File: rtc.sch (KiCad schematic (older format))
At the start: 0 parts

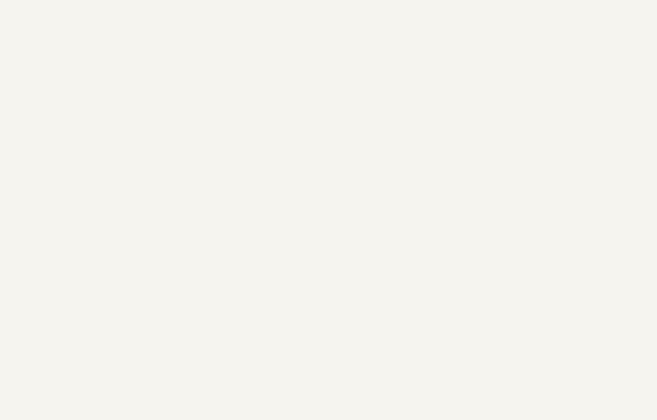
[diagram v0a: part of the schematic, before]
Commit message: Added some footprints. Basic board outline.
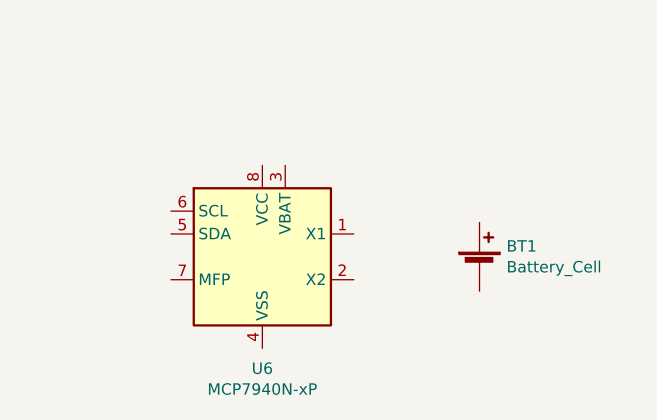
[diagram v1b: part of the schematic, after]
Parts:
- added BT1: Battery_Cell, Battery:BatteryHolder_Keystone_103_1x20mm, symbol Device:Battery_Cell
- added U6: MCP7940N-xP, Package_DIP:DIP-8_W7.62mm, symbol Timer:MCP7940N-xP
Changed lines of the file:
@@
 $Descr A4 11693 8268
 encoding utf-8
-Sheet 11 11
+Sheet 10 11
 Title "Neotron 32K"
 Date "2019-12-08"
@@
 Text HLabel 1400 1550 0    50   Input ~ 0
 MCU_I2C_SCL
+$Comp
+L Timer:MCP7940N-xP U6
+U 1 1 5E0F47D7
+P 5650 3350
+F 0 "U6" H 5650 2861 50  0000 C CNN
+F 1 "MCP7940N-xP" H 5650 2770 50  0000 C CNN
+F 2 "Package_DIP:DIP-8_W7.62mm" H 5650 3350 50  0001 C CNN
+F 3 "http://ww1.microchip.com/downloads/en/DeviceDoc/20005010F.pdf" H 5650 3350 50  0001 C CNN
+	1    5650 3350
+	1    0    0    -1
+$EndComp
+$Comp
+L Device:Battery_Cell BT1
+U 1 1 5E0F507E
+P 6600 3400
+F 0 "BT1" H 6718 3496 50  0000 L CNN
+F 1 "Battery_Cell" H 6718 3405 50  0000 L CNN
+F 2 "Battery:BatteryHolder_Keystone_103_1x20mm" V 6600 3460 50  0001 C CNN
+F 3 "~" V 6600 3460 50  0001 C CNN
+	1    6600 3400
+	1    0    0    -1
+$EndComp
 $EndSCHEMATC

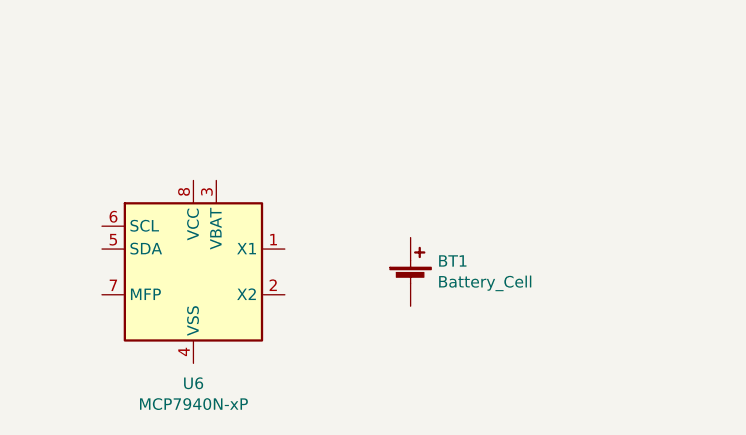
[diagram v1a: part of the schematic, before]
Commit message: Completed Power, SD, MIDI, Parallel and Joystick sheets.
Switch to sheet based 100x part numbering.
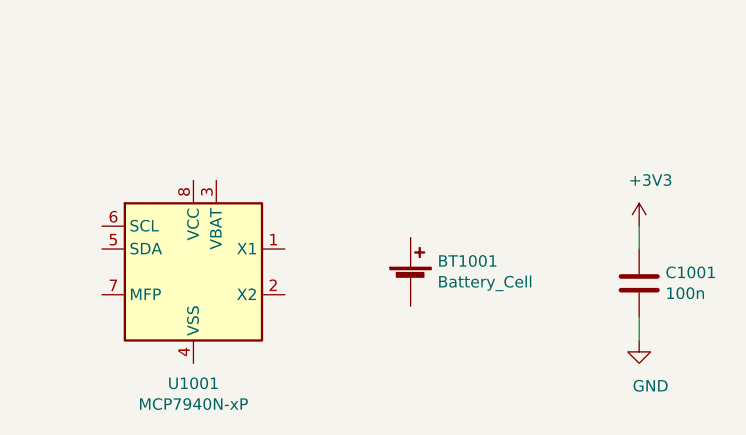
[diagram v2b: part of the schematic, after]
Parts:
- added C1001: 100n, Capacitor_THT:C_Disc_D3.0mm_W2.0mm_P2.50mm, symbol Device:C
- renumbered BT1 to BT1001, U6 to U1001
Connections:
- new net +3V3: C1001.1
- new net GND: C1001.2
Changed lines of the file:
@@
 MCU_I2C_SCL
 $Comp
-L Timer:MCP7940N-xP U6
+L Timer:MCP7940N-xP U1001
 U 1 1 5E0F47D7
 P 5650 3350
-F 0 "U6" H 5650 2861 50  0000 C CNN
+F 0 "U1001" H 5650 2861 50  0000 C CNN
 F 1 "MCP7940N-xP" H 5650 2770 50  0000 C CNN
 F 2 "Package_DIP:DIP-8_W7.62mm" H 5650 3350 50  0001 C CNN
@@
 $EndComp
 $Comp
-L Device:Battery_Cell BT1
+L Device:Battery_Cell BT1001
 U 1 1 5E0F507E
 P 6600 3400
-F 0 "BT1" H 6718 3496 50  0000 L CNN
+F 0 "BT1001" H 6718 3496 50  0000 L CNN
 F 1 "Battery_Cell" H 6718 3405 50  0000 L CNN
 F 2 "Battery:BatteryHolder_Keystone_103_1x20mm" V 6600 3460 50  0001 C CNN
@@
 	1    0    0    -1
 $EndComp
+$Comp
+L power:+3V3 #PWR?
+U 1 1 5E0203C5
+P 7600 3150
+AR Path="/5DF1D0B0/5E0203C5" Ref="#PWR?"  Part="1"
+AR Path="/5DF66898/5E0203C5" Ref="#PWR01001"  Part="1"
+F 0 "#PWR01001" H 7600 3000 50  0001 C CNN
+F 1 "+3V3" H 7650 3350 50  0000 C CNN
+F 2 "" H 7600 3150 50  0001 C CNN
+F 3 "" H 7600 3150 50  0001 C CNN
+	1    7600 3150
+	1    0    0    -1
+$EndComp
+$Comp
+L Device:C C?
+U 1 1 5E0203CB
+P 7600 3400
+AR Path="/5DF1D0B0/5E0203CB" Ref="C?"  Part="1"
+AR Path="/5DF66898/5E0203CB" Ref="C1001"  Part="1"
+F 0 "C1001" H 7715 3446 50  0000 L CNN
+F 1 "100n" H 7715 3355 50  0000 L CNN
+F 2 "Capacitor_THT:C_Disc_D3.0mm_W2.0mm_P2.50mm" H 7638 3250 50  0001 C CNN
+F 3 "~" H 7600 3400 50  0001 C CNN
+	1    7600 3400
+	1    0    0    -1
+$EndComp
+$Comp
+L power:GND #PWR?
+U 1 1 5E0203D1
+P 7600 3650
+AR Path="/5DF1D0B0/5E0203D1" Ref="#PWR?"  Part="1"
+AR Path="/5DF66898/5E0203D1" Ref="#PWR01002"  Part="1"
+F 0 "#PWR01002" H 7600 3400 50  0001 C CNN
+F 1 "GND" H 7650 3450 50  0000 C CNN
+F 2 "" H 7600 3650 50  0001 C CNN
+F 3 "" H 7600 3650 50  0001 C CNN
+	1    7600 3650
+	1    0    0    -1
+$EndComp
+Wire Wire Line
+	7600 3150 7600 3250
+Wire Wire Line
+	7600 3550 7600 3650
 $EndSCHEMATC

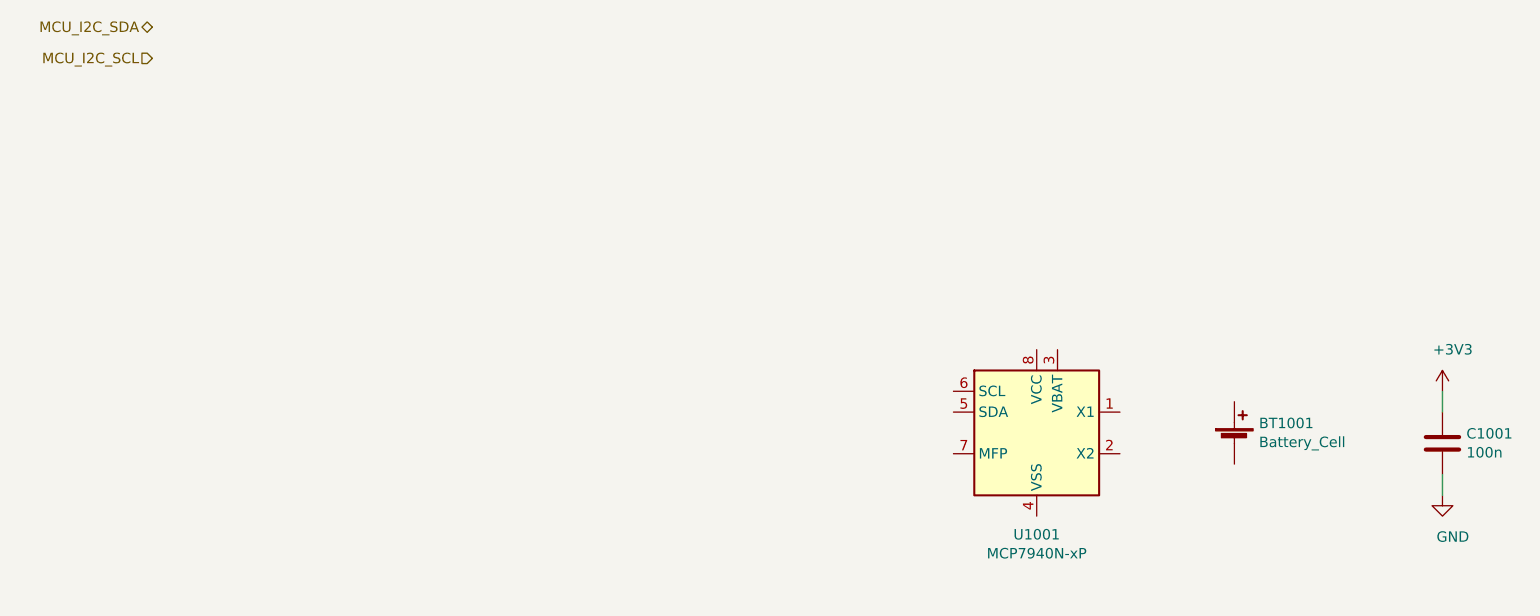
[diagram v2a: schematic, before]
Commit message: Schematic capture draft complete.
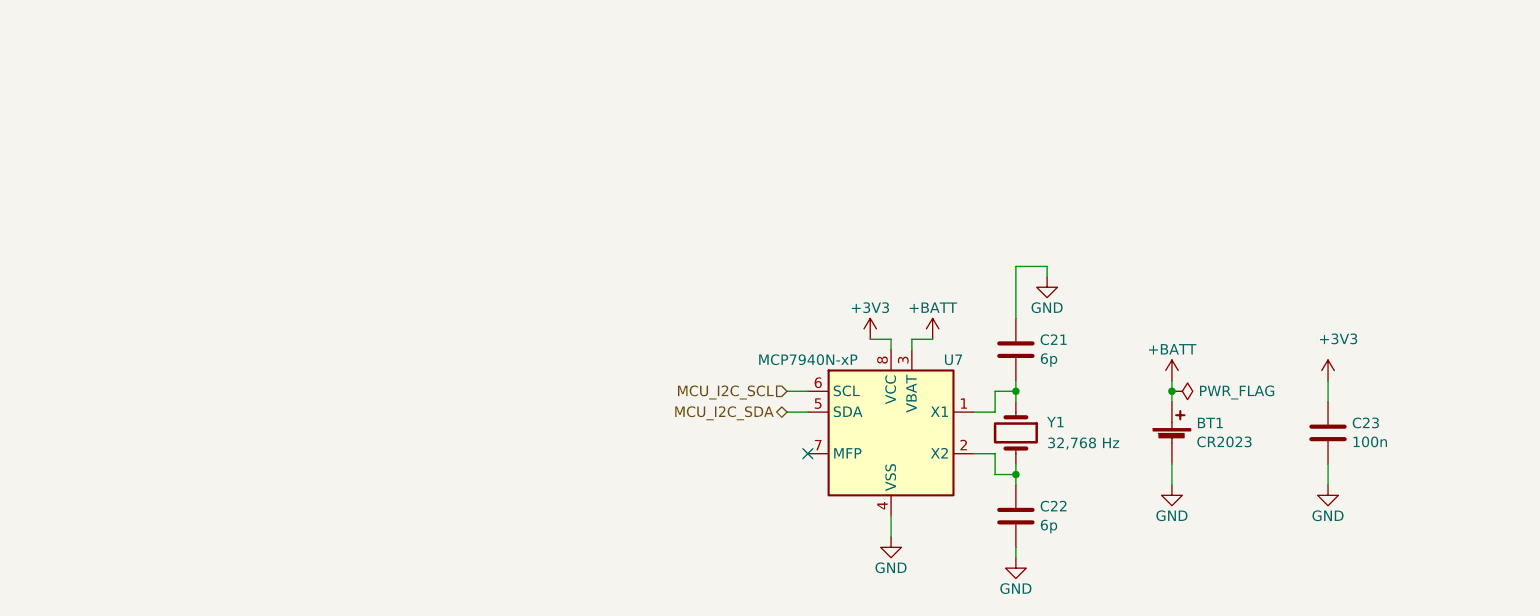
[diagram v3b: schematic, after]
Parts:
- added C21, C22: 6p, Capacitor_THT:C_Disc_D3.0mm_W2.0mm_P2.50mm, symbol Device:C
- added Y1: 32,768 Hz, Crystal:Crystal_C26-LF_D2.1mm_L6.5mm_Horizontal, symbol Device:Crystal
- BT1: renamed from BT1001; value Battery_Cell -> CR2023
- renumbered C1001 to C23, U1001 to U7
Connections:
- net +3V3: now also U7.8 (VCC)
- net GND: now also BT1.2 (-), U7.4 (VSS), C21.1, C22.2
- net MCU_I2C_SCL: now also U7.6 (SCL)
- net MCU_I2C_SDA: now also U7.5 (SDA)
- net at U7.1 (X1): now also C21.2, Y1.1
- net at U7.2 (X2): now also C22.1, Y1.2
- net +BATT: now reaches U7.3 (VBAT)
- net +BATT: now also BT1.1 (+)
- no-connect marks 0 -> 1
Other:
- moved on the sheet: BT1, C23, U7

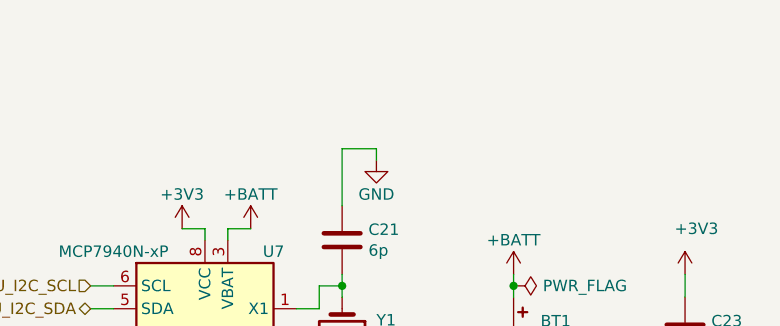
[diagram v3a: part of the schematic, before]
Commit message: Tidied up Atmega power. Added page titles.
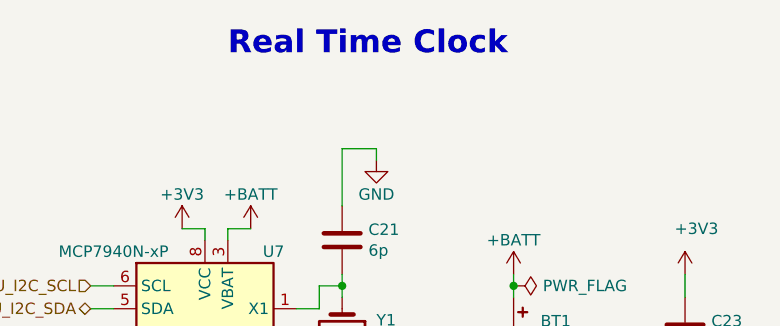
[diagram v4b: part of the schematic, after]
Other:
- note added: "Real Time Clock"
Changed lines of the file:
@@
 Sheet 8 10
 Title "Neotron 32K Main PCB"
-Date "2019-12-15"
-Rev "0.5"
+Date "2019-12-16"
+Rev "0.6"
 Comp "github.com/neotron-compute/Neotron-32-Hardware"
 Comment1 "Copyright (c) Jonathan 'theJPster' Pallant"
@@
 Wire Wire Line
 	6300 3150 6300 3200
+Text Notes 5050 2150 0    100  ~ 20
+Real Time Clock
 $EndSCHEMATC

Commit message: Work in progress.
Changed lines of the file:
@@
 AR Path="/5DF66898/5E0203C5" Ref="#PWR064"  Part="1"
 F 0 "#PWR064" H 7050 2950 50  0001 C CNN
-F 1 "+3V3" H 7100 3300 50  0000 C CNN
+F 1 "+3V3" H 7050 3250 50  0000 C CNN
 F 2 "" H 7050 3100 50  0001 C CNN
 F 3 "" H 7050 3100 50  0001 C CNN
